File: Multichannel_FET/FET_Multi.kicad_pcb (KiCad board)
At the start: 4 copper layers, 90 x 58 mm, 97 parts, among them J101 I2C, J102 DBT50G-9.5-4P, J103 DBT50G-9.5-4P, J104 Conn_01x04, J106 ADDR, J107 PU_ON, J108 PU_ON, J109 PU_ON, J110 PU_ON, J302 MC 4, J303 MC 4, Q101 IRF5210STRLPBF, Q102 IRF5210STRLPBF, Q103 IRF5210STRLPBF, Q104 IRF5210STRLPBF, U101 EL3H7(C)(TA)-G, U102 EL3H7(C)(TA)-G, U103 EL3H7(C)(TA)-G, U104 EL3H7(C)(TA)-G, U105 PCF8574T/3,518, U106 RCLAMP0524P-N, U301 EL3H7(C)(TA)-G, U302 EL3H7(C)(TA)-G, U303 EL3H7(C)(TA)-G, U304 EL3H7(C)(TA)-G

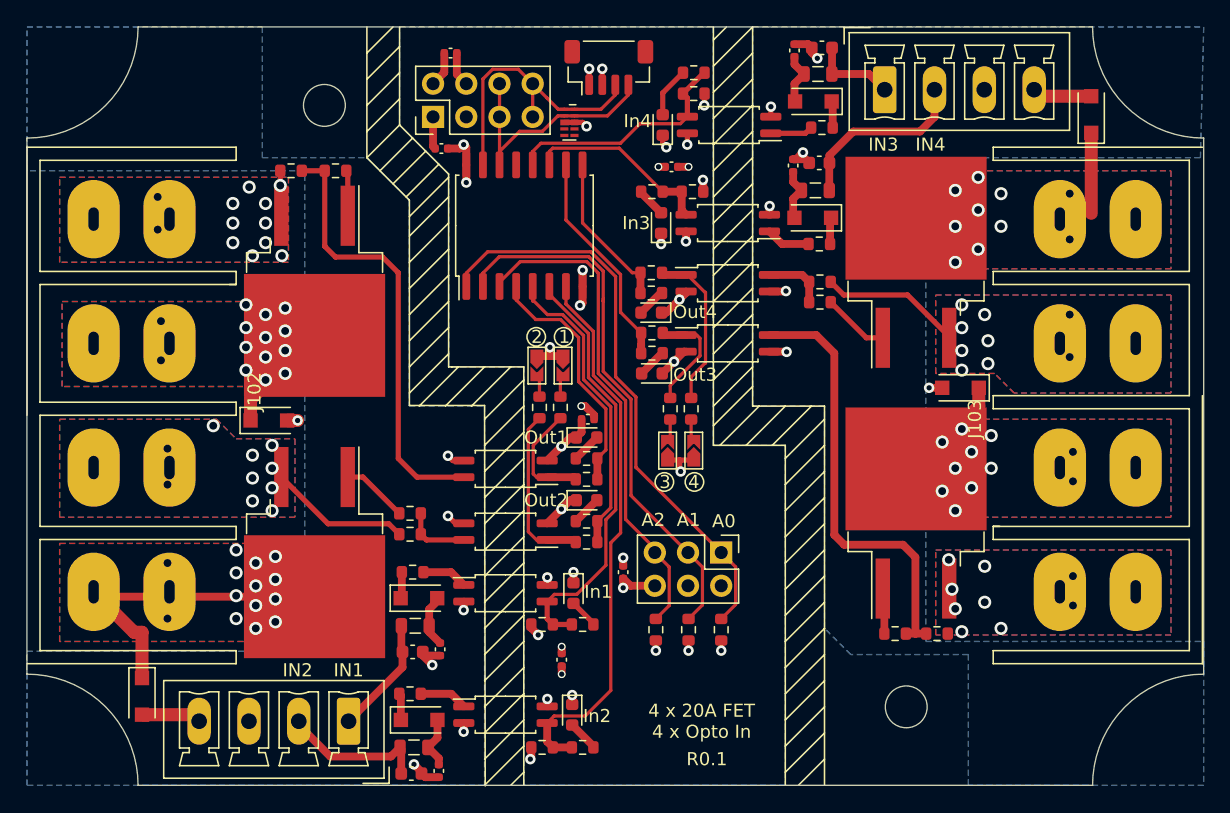
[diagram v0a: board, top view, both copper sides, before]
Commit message: Silkscreen Updates - MultiChannel_FET
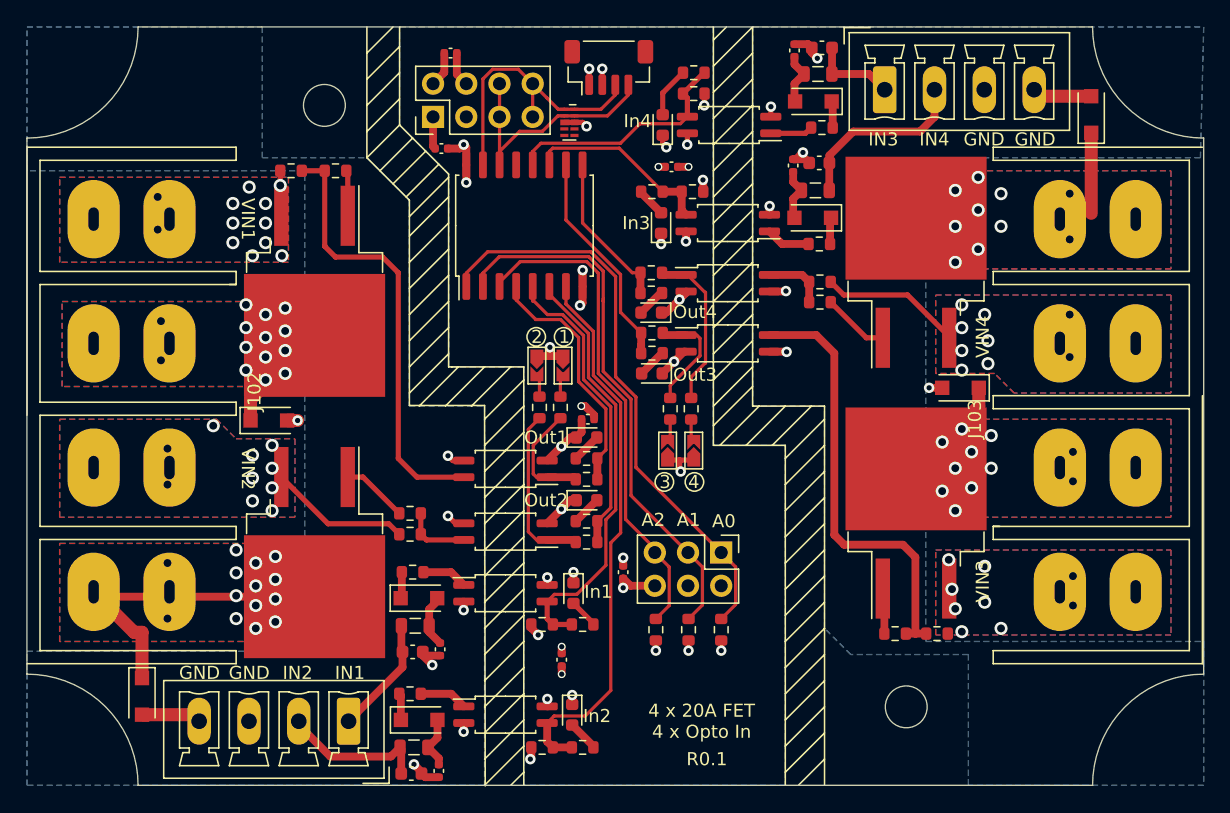
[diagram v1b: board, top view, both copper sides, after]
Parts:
- moved G*** 6.00 mm to (131.8, 70.0), turned to 180 degrees
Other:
- board text added: "3V3"
- board text added: "GND"
- board text added: "SCL"
- board text added: "SDA"
- board text added: "https://github.com/markfarnan/yacht_hardware"
